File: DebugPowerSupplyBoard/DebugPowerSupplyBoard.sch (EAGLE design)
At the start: 10 parts, among them IC1 LD117AV33, IC2 7805T

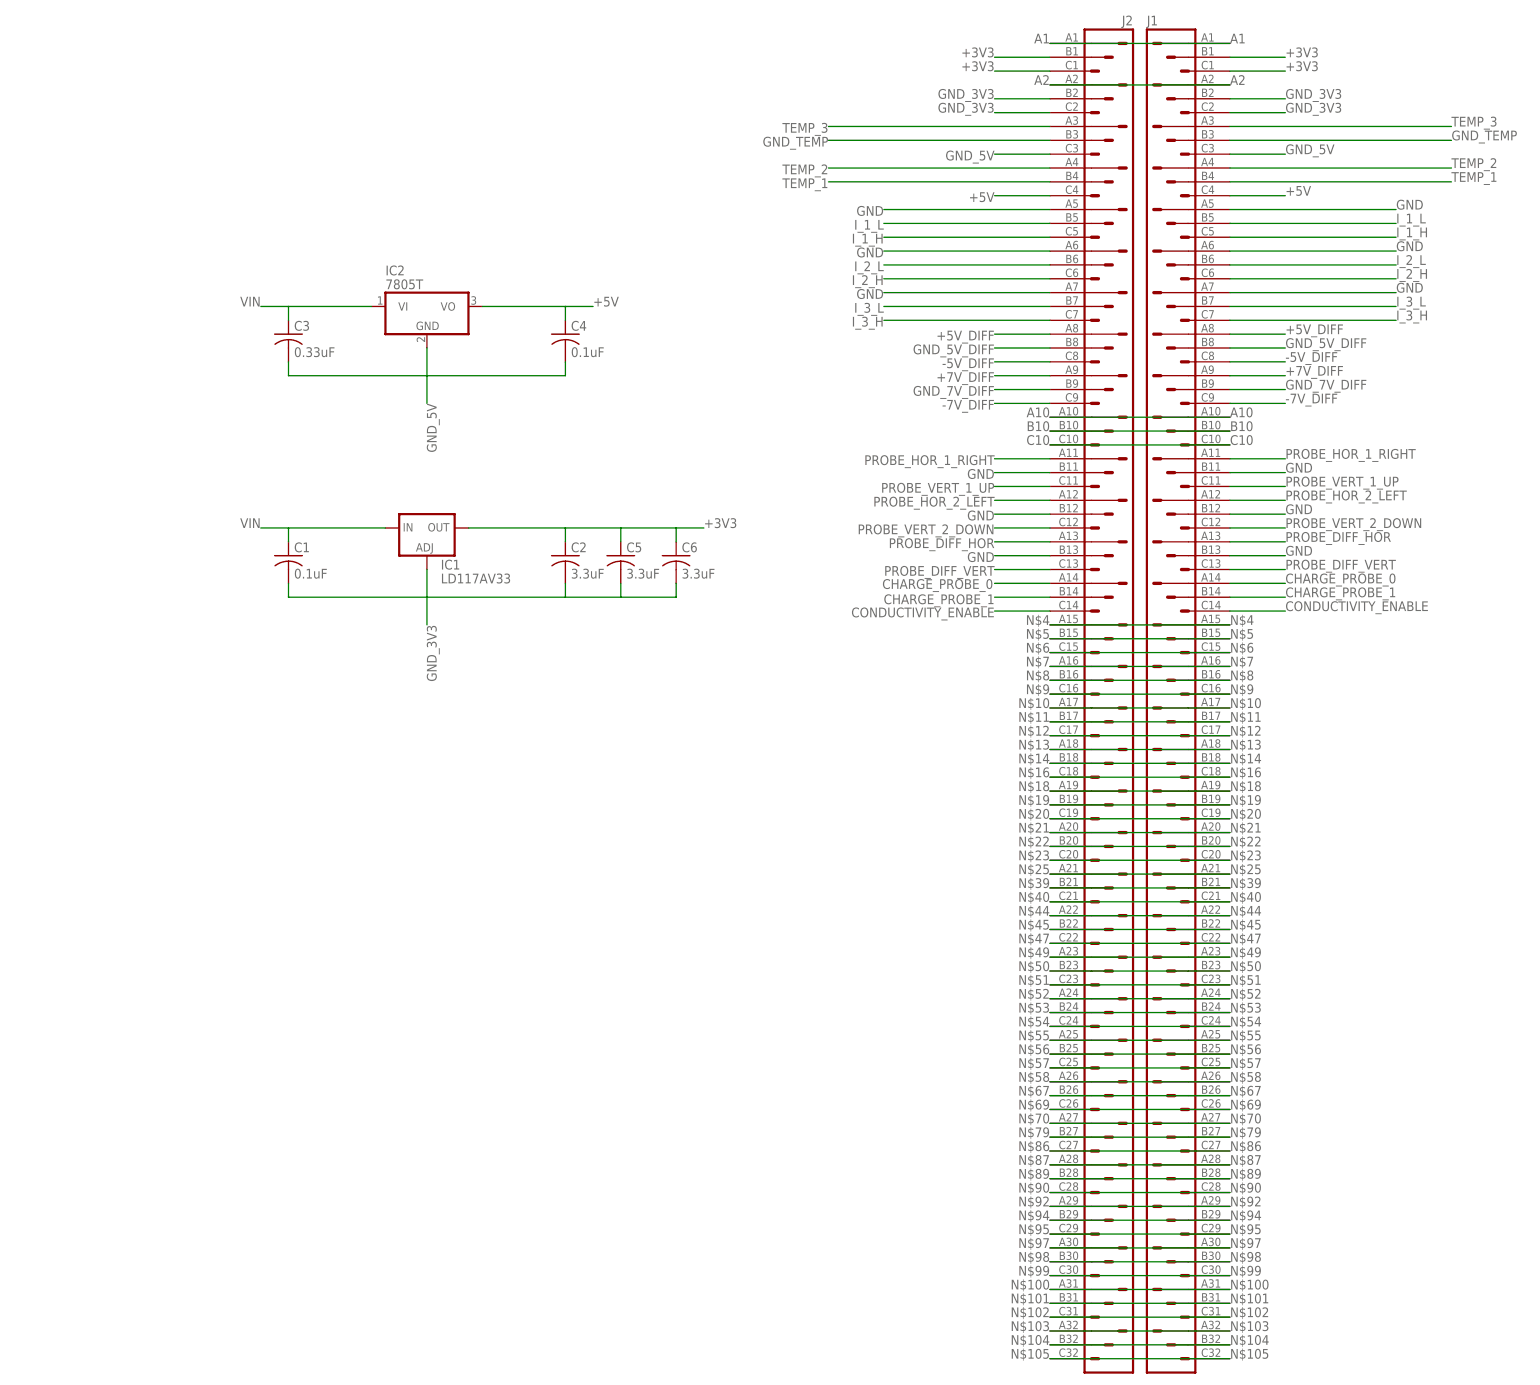
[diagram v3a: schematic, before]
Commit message: Added the XT60 connector. Almost done with this cursed board
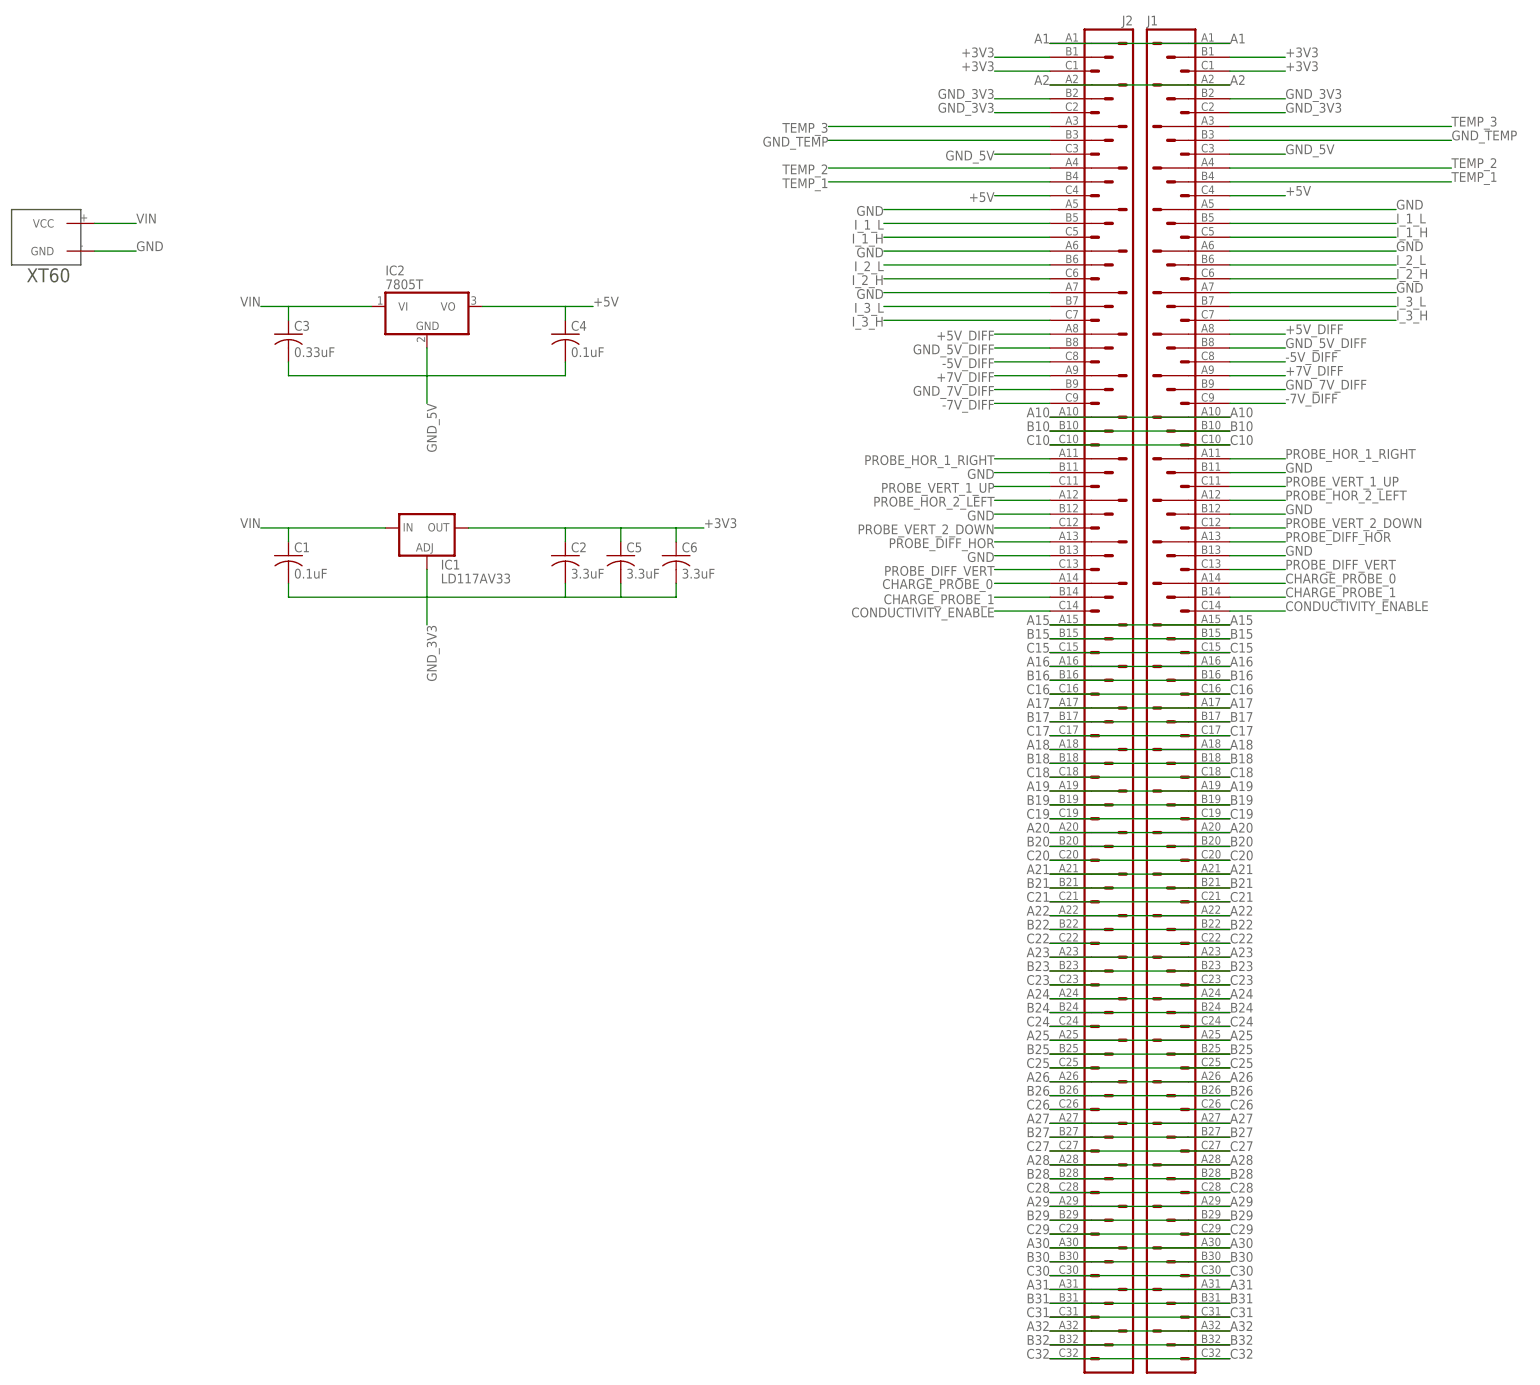
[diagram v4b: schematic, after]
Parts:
- added U$6: XT60, XT60:XT60
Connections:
- net N$10 renamed A17
- net N$100 renamed A31
- net N$101 renamed B31
- net N$102 renamed C31
- net N$103 renamed A32
- net N$104 renamed B32
- net N$105 renamed C32
- net N$11 renamed B17
- net N$12 renamed C17
- net N$13 renamed A18
- net N$14 renamed B18
- net N$16 renamed C18
- net N$18 renamed A19
- net N$19 renamed B19
- net N$20 renamed C19
- net N$21 renamed A20
- net N$22 renamed B20
- net N$23 renamed C20
- net N$25 renamed A21
- net N$39 renamed B21
- net N$4 renamed A15
- net N$40 renamed C21
- net N$44 renamed A22
- net N$45 renamed B22
- net N$47 renamed C22
- net N$49 renamed A23
- net N$5 renamed B15
- net N$50 renamed B23
- net N$51 renamed C23
- net N$52 renamed A24
- net N$53 renamed B24
- net N$54 renamed C24
- net N$55 renamed A25
- net N$56 renamed B25
- net N$57 renamed C25
- net N$58 renamed A26
- net N$6 renamed C15
- net N$67 renamed B26
- net N$69 renamed C26
- net N$7 renamed A16
- net N$70 renamed A27
- net N$79 renamed B27
- net N$8 renamed B16
- net N$86 renamed C27
- net N$87 renamed A28
- net N$89 renamed B28
- net N$9 renamed C16
- net N$90 renamed C28
- net N$92 renamed A29
- net N$94 renamed B29
- net N$95 renamed C29
- net N$97 renamed A30
- net N$98 renamed B30
- net N$99 renamed C30
- net GND: now also U$6.GND
- net VIN: now also U$6.VCC
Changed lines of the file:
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@@
 <part name="C5" library="rcl" deviceset="C-US" device="050-055X075" value="3.3uF"/>
 <part name="C6" library="rcl" deviceset="C-US" device="050-055X075" value="3.3uF"/>
+<part name="U$6" library="XT60" deviceset="XT60" device=""/>
 </parts>
 <sheets>
@@
 <instance part="C5" gate="G$1" x="-124.46" y="81.28"/>
 <instance part="C6" gate="G$1" x="-114.3" y="81.28"/>
+<instance part="U$6" gate="G$1" x="-226.06" y="139.7" rot="R180"/>
 </instances>
 <busses>
@@
 <pinref part="J1" gate="G$1" pin="B13"/>
 <label x="-2.54" y="81.28" size="1.778" layer="95"/>
+</segment>
+<segment>
+<pinref part="U$6" gate="G$1" pin="GND"/>
+<wire x1="-220.98" y1="137.16" x2="-213.36" y2="137.16" width="0.1524" layer="91"/>
+<label x="-213.36" y="137.16" size="1.778" layer="95"/>
 </segment>
 </net>
@@
 <wire x1="-185.42" y1="127" x2="-190.5" y2="127" width="0.1524" layer="91"/>
 <label x="-190.5" y="127" size="1.778" layer="95" rot="MR0"/>
+</segment>
+<segment>
+<pinref part="U$6" gate="G$1" pin="VCC"/>
+<wire x1="-220.98" y1="142.24" x2="-213.36" y2="142.24" width="0.1524" layer="91"/>
+<label x="-213.36" y="142.24" size="1.778" layer="95"/>
 </segment>
 </net>
@@
 </segment>
 </net>
-<net name="N$4" class="0">
+<net name="A15" class="0">
 <segment>
 <pinref part="J2" gate="G$1" pin="A15"/>
@@
 </segment>
 </net>
-<net name="N$5" class="0">
+<net name="B15" class="0">
 <segment>
 <pinref part="J2" gate="G$1" pin="B15"/>
@@
 </segment>
 </net>
-<net name="N$6" class="0">
+<net name="C15" class="0">
 <segment>
 <pinref part="J2" gate="G$1" pin="C15"/>
@@
 </segment>
 </net>
-<net name="N$7" class="0">
+<net name="A16" class="0">
 <segment>
 <pinref part="J1" gate="G$1" pin="A16"/>
@@
 </segment>
 </net>
-<net name="N$8" class="0">
+<net name="B16" class="0">
 <segment>
 <pinref part="J2" gate="G$1" pin="B16"/>
@@
 </segment>
 </net>
-<net name="N$9" class="0">
+<net name="C16" class="0">
 <segment>
 <pinref part="J1" gate="G$1" pin="C16"/>
@@
 </segment>
 </net>
-<net name="N$10" class="0">
+<net name="A17" class="0">
 <segment>
 <pinref part="J2" gate="G$1" pin="A17"/>
@@
 </segment>
 </net>
-<net name="N$11" class="0">
+<net name="B17" class="0">
 <segment>
 <pinref part="J1" gate="G$1" pin="B17"/>
@@
 </segment>
 </net>
-<net name="N$12" class="0">
+<net name="C17" class="0">
 <segment>
 <pinref part="J2" gate="G$1" pin="C17"/>
@@
 </segment>
 </net>
-<net name="N$13" class="0">
+<net name="A18" class="0">
 <segment>
 <pinref part="J1" gate="G$1" pin="A18"/>
@@
 </segment>
 </net>
-<net name="N$14" class="0">
+<net name="B18" class="0">
 <segment>
 <pinref part="J2" gate="G$1" pin="B18"/>
@@
 </segment>
 </net>
-<net name="N$16" class="0">
+<net name="C18" class="0">
 <segment>
 <pinref part="J1" gate="G$1" pin="C18"/>
@@
 </segment>
 </net>
-<net name="N$18" class="0">
+<net name="A19" class="0">
 <segment>
 <pinref part="J2" gate="G$1" pin="A19"/>
@@
 </segment>
 </net>
-<net name="N$19" class="0">
+<net name="B19" class="0">
 <segment>
 <pinref part="J1" gate="G$1" pin="B19"/>
@@
 </segment>
 </net>
-<net name="N$20" class="0">
+<net name="C19" class="0">
 <segment>
 <pinref part="J2" gate="G$1" pin="C19"/>
@@
 </segment>
 </net>
-<net name="N$21" class="0">
+<net name="A20" class="0">
 <segment>
 <pinref part="J1" gate="G$1" pin="A20"/>
@@
 </segment>
 </net>
-<net name="N$22" class="0">
+<net name="B20" class="0">
 <segment>
 <pinref part="J2" gate="G$1" pin="B20"/>
@@
 </segment>
 </net>
-<net name="N$23" class="0">
+<net name="C20" class="0">
 <segment>
 <pinref part="J1" gate="G$1" pin="C20"/>
@@
 </segment>
 </net>
-<net name="N$25" class="0">
+<net name="A21" class="0">
 <segment>
 <pinref part="J2" gate="G$1" pin="A21"/>
@@
 </segment>
 </net>
-<net name="N$39" class="0">
+<net name="B21" class="0">
 <segment>
 <pinref part="J1" gate="G$1" pin="B21"/>
@@
 </segment>
 </net>
-<net name="N$40" class="0">
+<net name="C21" class="0">
 <segment>
 <pinref part="J2" gate="G$1" pin="C21"/>
@@
 </segment>
 </net>
-<net name="N$44" class="0">
+<net name="A22" class="0">
 <segment>
 <pinref part="J1" gate="G$1" pin="A22"/>
@@
 </segment>
 </net>
-<net name="N$45" class="0">
+<net name="B22" class="0">
 <segment>
 <pinref part="J2" gate="G$1" pin="B22"/>
@@
 </segment>
 </net>
-<net name="N$47" class="0">
+<net name="C22" class="0">
 <segment>
 <pinref part="J1" gate="G$1" pin="C22"/>
@@
 </segment>
 </net>
-<net name="N$49" class="0">
+<net name="A23" class="0">
 <segment>
 <pinref part="J2" gate="G$1" pin="A23"/>
@@
 </segment>
 </net>
-<net name="N$50" class="0">
+<net name="B23" class="0">
 <segment>
 <pinref part="J1" gate="G$1" pin="B23"/>
@@
 </segment>
 </net>
-<net name="N$51" class="0">
+<net name="C23" class="0">
 <segment>
 <pinref part="J2" gate="G$1" pin="C23"/>
@@
 </segment>
 </net>
-<net name="N$52" class="0">
+<net name="A24" class="0">
 <segment>
 <pinref part="J2" gate="G$1" pin="A24"/>
@@
 </segment>
 </net>
-<net name="N$53" class="0">
+<net name="B24" class="0">
 <segment>
 <pinref part="J1" gate="G$1" pin="B24"/>
@@
 </segment>
 </net>
-<net name="N$54" class="0">
+<net name="C24" class="0">
 <segment>
 <pinref part="J2" gate="G$1" pin="C24"/>
@@
 </segment>
 </net>
-<net name="N$55" class="0">
+<net name="A25" class="0">
 <segment>
 <pinref part="J1" gate="G$1" pin="A25"/>
@@
 </segment>
 </net>
-<net name="N$56" class="0">
+<net name="B25" class="0">
 <segment>
 <pinref part="J2" gate="G$1" pin="B25"/>
@@
 </segment>
 </net>
-<net name="N$57" class="0">
+<net name="C25" class="0">
 <segment>
 <pinref part="J1" gate="G$1" pin="C25"/>
@@
 </segment>
 </net>
-<net name="N$58" class="0">
+<net name="A26" class="0">
 <segment>
 <pinref part="J2" gate="G$1" pin="A26"/>
@@
 </segment>
 </net>
-<net name="N$67" class="0">
+<net name="B26" class="0">
 <segment>
 <pinref part="J1" gate="G$1" pin="B26"/>
@@
 </segment>
 </net>
-<net name="N$69" class="0">
+<net name="C26" class="0">
 <segment>
 <pinref part="J2" gate="G$1" pin="C26"/>
@@
 </segment>
 </net>
-<net name="N$70" class="0">
+<net name="A27" class="0">
 <segment>
 <pinref part="J1" gate="G$1" pin="A27"/>
@@
 </segment>
 </net>
-<net name="N$79" class="0">
+<net name="B27" class="0">
 <segment>
 <pinref part="J2" gate="G$1" pin="B27"/>
@@
 </segment>
 </net>
-<net name="N$86" class="0">
+<net name="C27" class="0">
 <segment>
 <pinref part="J2" gate="G$1" pin="C27"/>
@@
 </segment>
 </net>
-<net name="N$87" class="0">
+<net name="A28" class="0">
 <segment>
 <pinref part="J1" gate="G$1" pin="A28"/>
@@
 </segment>
 </net>
-<net name="N$89" class="0">
+<net name="B28" class="0">
 <segment>
 <pinref part="J2" gate="G$1" pin="B28"/>
@@
 </segment>
 </net>
-<net name="N$90" class="0">
+<net name="C28" class="0">
 <segment>
 <pinref part="J1" gate="G$1" pin="C28"/>
@@
 </segment>
 </net>
-<net name="N$92" class="0">
+<net name="A29" class="0">
 <segment>
 <pinref part="J2" gate="G$1" pin="A29"/>
@@
 </segment>
 </net>
-<net name="N$94" class="0">
+<net name="B29" class="0">
 <segment>
 <pinref part="J1" gate="G$1" pin="B29"/>
@@
 </segment>
 </net>
-<net name="N$95" class="0">
+<net name="C29" class="0">
 <segment>
 <pinref part="J2" gate="G$1" pin="C29"/>
@@
 </segment>
 </net>
-<net name="N$97" class="0">
+<net name="A30" class="0">
 <segment>
 <pinref part="J1" gate="G$1" pin="A30"/>
@@
 </segment>
 </net>
-<net name="N$98" class="0">
+<net name="B30" class="0">
 <segment>
 <pinref part="J2" gate="G$1" pin="B30"/>
@@
 </segment>
 </net>
-<net name="N$99" class="0">
+<net name="C30" class="0">
 <segment>
 <pinref part="J1" gate="G$1" pin="C30"/>
@@
 </segment>
 </net>
-<net name="N$100" class="0">
+<net name="A31" class="0">
 <segment>
 <pinref part="J2" gate="G$1" pin="A31"/>
@@
 </segment>
 </net>
-<net name="N$101" class="0">
+<net name="B31" class="0">
 <segment>
 <pinref part="J1" gate="G$1" pin="B31"/>
@@
 </segment>
 </net>
-<net name="N$102" class="0">
+<net name="C31" class="0">
 <segment>
 <pinref part="J2" gate="G$1" pin="C31"/>
@@
 </segment>
 </net>
-<net name="N$103" class="0">
+<net name="A32" class="0">
 <segment>
 <pinref part="J1" gate="G$1" pin="A32"/>
@@
 </segment>
 </net>
-<net name="N$104" class="0">
+<net name="B32" class="0">
 <segment>
 <pinref part="J2" gate="G$1" pin="B32"/>
@@
 </segment>
 </net>
-<net name="N$105" class="0">
+<net name="C32" class="0">
 <segment>
 <pinref part="J1" gate="G$1" pin="C32"/>
